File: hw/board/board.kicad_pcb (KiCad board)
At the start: 2 copper layers, 31.8 x 54.6 mm, 4 parts, among them J1 Conn_02x20_Odd_Even, U1 W65C02S

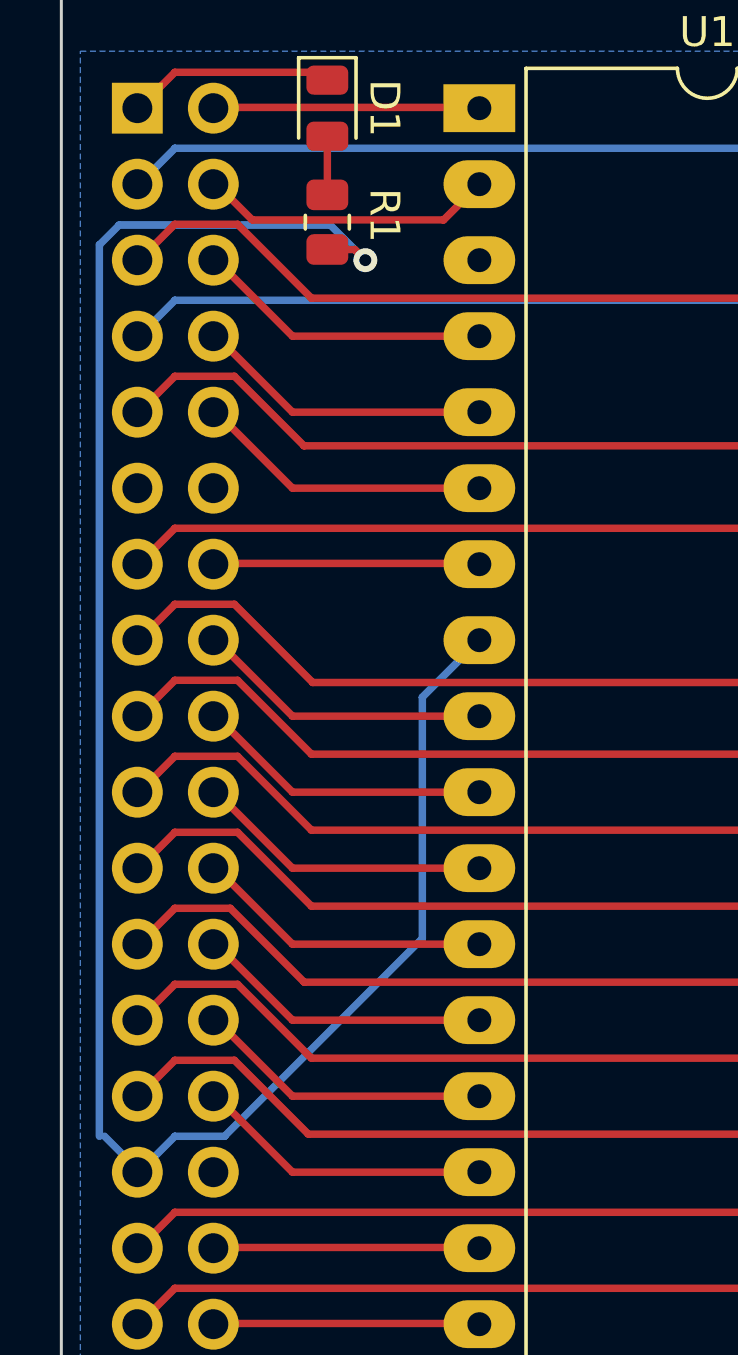
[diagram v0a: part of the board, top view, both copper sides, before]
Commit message: Fix ground plane not connected
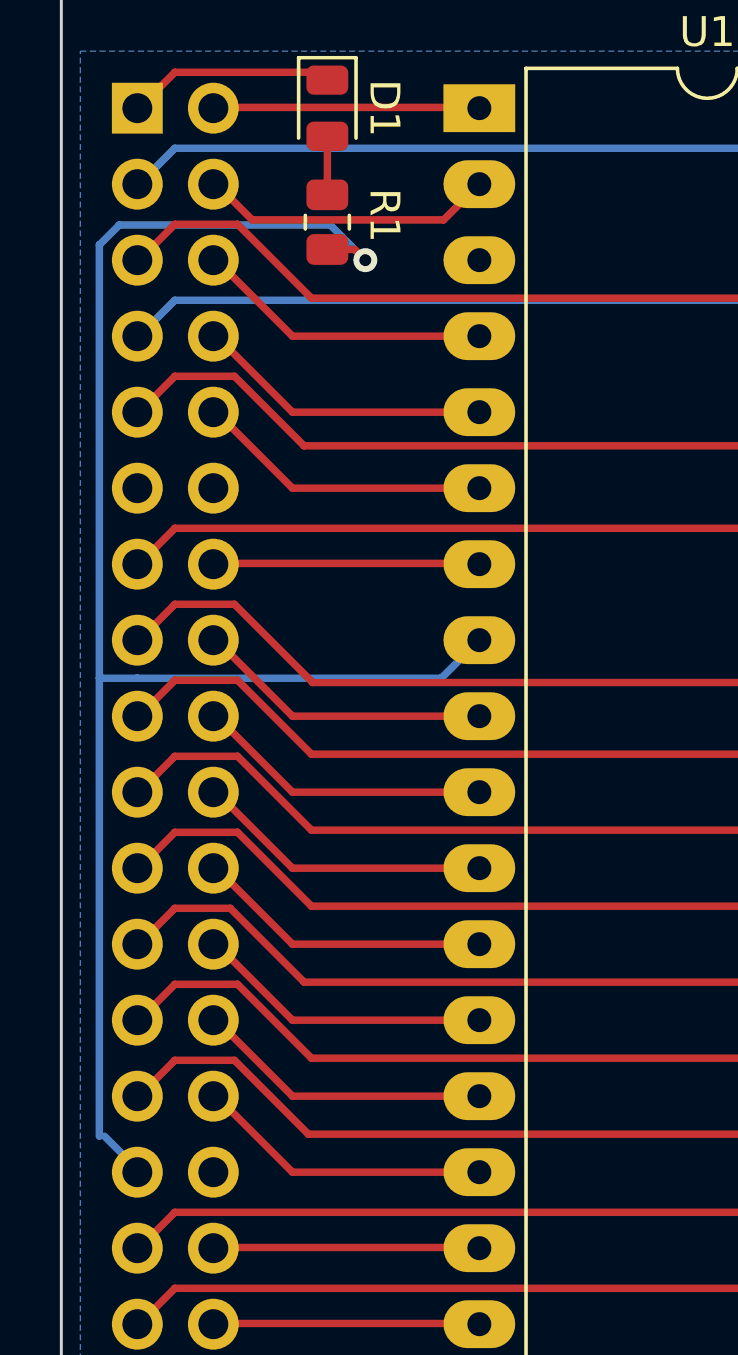
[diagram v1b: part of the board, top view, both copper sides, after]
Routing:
- net +3V3: track 66.0 -> 55.7 mm
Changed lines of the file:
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@@
       (svguseinch false)
       (svgprecision 6)
-      (excludeedgelayer true)
+      (excludeedgelayer false)
       (plotframeref false)
       (viasonmask false)
@@
       (psa4output false)
       (plotreference true)
-      (plotvalue true)
+      (plotvalue false)
       (plotinvisibletext false)
       (sketchpadsonfab false)
-      (subtractmaskfromsilk false)
+      (subtractmaskfromsilk true)
       (outputformat 1)
       (mirror false)
-      (drillshape 1)
+      (drillshape 0)
       (scaleselection 1)
-      (outputdirectory "")
+      (outputdirectory "output/")
     )
   )
@@
     (fp_line (start 1 0.625) (end -1 0.625) (layer "F.Fab") (width 0.1))
     (fp_line (start -1 -0.625) (end 1 -0.625) (layer "F.Fab") (width 0.1))
-    (pad "1" smd roundrect (at -0.9125 0 90) (size 1.025 1.4) (layers "F.Cu" "F.Paste" "F.Mask") (roundrect_rratio 0.243902)
+    (pad "1" smd roundrect (at -0.9125 0 90) (size 1.025 1.4) (layers "F.Cu" "F.Paste" "F.Mask") (roundrect_rratio 0.243902439)
       (net 30 "+3V3") (pintype "passive"))
-    (pad "2" smd roundrect (at 0.9125 0 90) (size 1.025 1.4) (layers "F.Cu" "F.Paste" "F.Mask") (roundrect_rratio 0.243902)
+    (pad "2" smd roundrect (at 0.9125 0 90) (size 1.025 1.4) (layers "F.Cu" "F.Paste" "F.Mask") (roundrect_rratio 0.243902439)
       (net 2 "Net-(D1-Pad2)") (pintype "passive"))
     (model "${KICAD6_3DMODEL_DIR}/Resistor_SMD.3dshapes/R_0805_2012Metric.wrl"
@@
   (segment (start 91.0825 64.4125) (end 91.44 64.77) (width 0.25) (layer "F.Cu") (net 30))
   (via (at 91.44 64.77) (size 0.8) (drill 0.4) (layers "F.Cu" "B.Cu") (net 30))
-  (segment (start 85.074511 94.050489) (end 86.735521 94.050489) (width 0.25) (layer "B.Cu") (net 30))
-  (segment (start 93.345 79.375) (end 95.25 77.47) (width 0.25) (layer "B.Cu") (net 30))
-  (segment (start 86.735521 94.050489) (end 93.345 87.44101) (width 0.25) (layer "B.Cu") (net 30))
+  (segment (start 93.98 78.74) (end 83.82 78.74) (width 0.25) (layer "B.Cu") (net 30))
+  (segment (start 95.25 77.47) (end 93.98 78.74) (width 0.25) (layer "B.Cu") (net 30))
   (segment (start 90.265489 63.595489) (end 91.44 64.77) (width 0.25) (layer "B.Cu") (net 30))
   (segment (start 82.55 64.258501) (end 82.55 94.050489) (width 0.25) (layer "B.Cu") (net 30))
   (segment (start 83.213012 63.595489) (end 90.265489 63.595489) (width 0.25) (layer "B.Cu") (net 30))
+  (segment (start 83.82 78.74) (end 82.55 78.74) (width 0.25) (layer "B.Cu") (net 30))
   (segment (start 82.725489 94.050489) (end 83.9 95.225) (width 0.25) (layer "B.Cu") (net 30))
-  (segment (start 93.345 87.44101) (end 93.345 79.375) (width 0.25) (layer "B.Cu") (net 30))
-  (segment (start 83.9 95.225) (end 85.074511 94.050489) (width 0.25) (layer "B.Cu") (net 30))
   (segment (start 82.55 64.258501) (end 83.213012 63.595489) (width 0.25) (layer "B.Cu") (net 30))
   (segment (start 85.074511 96.590489) (end 109.149511 96.590489) (width 0.25) (layer "F.Cu") (net 31))

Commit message: add basic stuff to board
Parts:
- removed D1: LED, LED_SMD:LED_0805_2012Metric
- added C1: 100n, Capacitor_SMD:C_0603_1608Metric_Pad1.08x0.95mm_HandSolder, B.Cu at (143.3, 59.0)
- added C10: 4.7u, Capacitor_SMD:C_0603_1608Metric_Pad1.08x0.95mm_HandSolder, B.Cu at (106.2, 64.4)
- added C11: 100n, Capacitor_SMD:C_0603_1608Metric_Pad1.08x0.95mm_HandSolder, B.Cu at (107.8, 64.4)
- added C12: 4.7u, Capacitor_SMD:C_0603_1608Metric_Pad1.08x0.95mm_HandSolder, B.Cu at (119.0, 57.4)
- added C13: 100n, Capacitor_SMD:C_0603_1608Metric_Pad1.08x0.95mm_HandSolder, B.Cu at (121.4, 65.2)
- added C14: 100n, Capacitor_SMD:C_0603_1608Metric_Pad1.08x0.95mm_HandSolder, B.Cu at (111.4, 57.4)
- added C15: 100n, Capacitor_SMD:C_0603_1608Metric_Pad1.08x0.95mm_HandSolder, B.Cu at (110.6, 65.5)
- added C16: 4.7u, Capacitor_SMD:C_0603_1608Metric_Pad1.08x0.95mm_HandSolder, F.Cu at (126.8, 59.9)
- added C17: 100n, Capacitor_SMD:C_0603_1608Metric_Pad1.08x0.95mm_HandSolder, B.Cu at (115.0, 68.4)
- added C18: 100n, Capacitor_SMD:C_0603_1608Metric_Pad1.08x0.95mm_HandSolder, B.Cu at (118.4, 68.4)
- added C19: 100n, Capacitor_SMD:C_0603_1608Metric_Pad1.08x0.95mm_HandSolder, B.Cu at (121.4, 61.2)
- added C2: 100n, Capacitor_SMD:C_0603_1608Metric_Pad1.08x0.95mm_HandSolder, B.Cu at (143.4, 63.5)
- added C20: 100n, Capacitor_SMD:C_0603_1608Metric_Pad1.08x0.95mm_HandSolder, B.Cu at (115.6, 57.4)
- added C21: 4.7u, Capacitor_SMD:C_0603_1608Metric_Pad1.08x0.95mm_HandSolder, B.Cu at (106.2, 61.0)
- added C22: 100n, Capacitor_SMD:C_0603_1608Metric_Pad1.08x0.95mm_HandSolder, B.Cu at (107.8, 61.0)
- added C23: 4.7u, Capacitor_SMD:C_0603_1608Metric_Pad1.08x0.95mm_HandSolder, B.Cu at (160.4, 54.4)
- added C24: 0.1u, Capacitor_SMD:C_0603_1608Metric_Pad1.08x0.95mm_HandSolder, B.Cu at (158.8, 54.4)
- added C25: 10u, Capacitor_SMD:C_0603_1608Metric_Pad1.08x0.95mm_HandSolder, F.Cu at (123.8, 26.4)
- added C26: 1u, Capacitor_SMD:C_0603_1608Metric_Pad1.08x0.95mm_HandSolder, F.Cu at (125.3, 26.4)
- added C27: 10n, Capacitor_SMD:C_0603_1608Metric_Pad1.08x0.95mm_HandSolder, F.Cu at (135.8, 24.1)
- added C28: 4.7u, Capacitor_SMD:C_0603_1608Metric_Pad1.08x0.95mm_HandSolder, F.Cu at (119.4, 54.5)
- added C29: 2.2u, Capacitor_SMD:C_0603_1608Metric_Pad1.08x0.95mm_HandSolder, F.Cu at (162.4, 25.6)
- added C3: 100n, Capacitor_SMD:C_0603_1608Metric_Pad1.08x0.95mm_HandSolder, B.Cu at (148.9, 70.0)
- added C30: 1u, Capacitor_SMD:C_0603_1608Metric_Pad1.08x0.95mm_HandSolder, F.Cu at (163.0, 37.9)
- added C31: 100n, Capacitor_SMD:C_0603_1608Metric_Pad1.08x0.95mm_HandSolder, F.Cu at (162.9, 36.2)
- added C32: 10n, Capacitor_SMD:C_0603_1608Metric_Pad1.08x0.95mm_HandSolder, F.Cu at (163.0, 39.5)
- added C33: 0.1u, Capacitor_SMD:C_0603_1608Metric_Pad1.08x0.95mm_HandSolder, F.Cu at (118.6, 51.4)
- added C34: LOAD, Capacitor_SMD:C_0603_1608Metric_Pad1.08x0.95mm_HandSolder, F.Cu at (109.6, 51.8)
- added C35: LOAD, Capacitor_SMD:C_0603_1608Metric_Pad1.08x0.95mm_HandSolder, F.Cu at (104.4, 51.8)
- added C4: 100n, Capacitor_SMD:C_0603_1608Metric_Pad1.08x0.95mm_HandSolder, B.Cu at (152.9, 70.0)
- added C5: 100n, Capacitor_SMD:C_0603_1608Metric_Pad1.08x0.95mm_HandSolder, B.Cu at (159.9, 64.6)
- added C6: 100n, Capacitor_SMD:C_0603_1608Metric_Pad1.08x0.95mm_HandSolder, B.Cu at (159.7, 59.2)
- added C7: 100n, Capacitor_SMD:C_0603_1608Metric_Pad1.08x0.95mm_HandSolder, B.Cu at (152.7, 53.7)
- added C8: 100n, Capacitor_SMD:C_0603_1608Metric_Pad1.08x0.95mm_HandSolder, B.Cu at (151.2, 54.2)
- added C9: 100n, Capacitor_SMD:C_0603_1608Metric_Pad1.08x0.95mm_HandSolder, B.Cu at (149.6, 53.6)
- added L1: 600R @ 100MHz, Inductor_SMD:L_0603_1608Metric_Pad1.05x0.95mm_HandSolder, B.Cu at (104.6, 64.4)
- added L2: 600R @ 100MHz, Inductor_SMD:L_0603_1608Metric_Pad1.05x0.95mm_HandSolder, B.Cu at (104.6, 61.0)
- added L3: 600R @ 100MHz, Inductor_SMD:L_0603_1608Metric_Pad1.05x0.95mm_HandSolder, B.Cu at (157.2, 54.4)
- added R10: 10k, Resistor_SMD:R_0603_1608Metric_Pad0.98x0.95mm_HandSolder, F.Cu at (117.8, 54.5)
- added R11: 4.7k, Resistor_SMD:R_0603_1608Metric_Pad0.98x0.95mm_HandSolder, F.Cu at (116.4, 54.5)
- added R12: 10k, Resistor_SMD:R_0603_1608Metric_Pad0.98x0.95mm_HandSolder, F.Cu at (114.8, 54.5)
- added R2: 5.1k, Resistor_SMD:R_0603_1608Metric_Pad0.98x0.95mm_HandSolder, B.Cu at (94.8, 62.1)
- added R3: 10k, Resistor_SMD:R_0603_1608Metric_Pad0.98x0.95mm_HandSolder, F.Cu at (117.8, 71.5)
- added R4: 12k 1%, Resistor_SMD:R_0603_1608Metric_Pad0.98x0.95mm_HandSolder, B.Cu at (113.6, 61.5)
- added R5: R, Resistor_SMD:R_0603_1608Metric_Pad0.98x0.95mm_HandSolder, F.Cu at (107.5, 65.7)
- added R6: 10k, Resistor_SMD:R_0603_1608Metric_Pad0.98x0.95mm_HandSolder, F.Cu at (120.9, 46.2)
- added R7: 10k, Resistor_SMD:R_0603_1608Metric_Pad0.98x0.95mm_HandSolder, F.Cu at (115.9, 46.5)
- added R8: 10k, Resistor_SMD:R_0603_1608Metric_Pad0.98x0.95mm_HandSolder, F.Cu at (115.9, 50.0)
- added R9: 2.2k, Resistor_SMD:R_0603_1608Metric_Pad0.98x0.95mm_HandSolder, F.Cu at (122.7, 48.9)
- added U2: LD1117S33TR_SOT223, Package_TO_SOT_SMD:SOT-223-3_TabPin2, F.Cu at (130.6, 24.9)
- added U3: LD1117S12TR_SOT223, Package_TO_SOT_SMD:SOT-223-3_TabPin2, F.Cu at (163.8, 30.9)
- added U4: FT2232HL, Package_QFP:LQFP-64_10x10mm_P0.5mm, F.Cu at (116.0, 63.0)
- added U5: 93LCxxBxxOT, Package_TO_SOT_SMD:SOT-23-6, F.Cu at (118.9, 48.8)
- added Y1: 12MHz, Crystal:Crystal_SMD_5032-2Pin_5.0x3.2mm_HandSoldering, F.Cu at (107.0, 54.6)
- J1: value Conn_02x20_Odd_Even -> USB_C_Receptacle_USB2.0; footprint Connector_PinSocket_2.54mm:PinSocket_2x20_P2.54mm_Vertical -> Connector_USB:USB_C_Receptacle_GCT_USB4085; moved to F.Cu
- R1: value 100 -> 5.1k; footprint Resistor_SMD:R_0805_2012Metric -> Resistor_SMD:R_0603_1608Metric_Pad0.98x0.95mm_HandSolder; moved to B.Cu
- U1: value W65C02S -> T8Q144; footprint Package_DIP:DIP-40_W15.24mm_LongPads -> Package_QFP:LQFP-144_20x20mm_P0.5mm
- moved U1 56.4 mm to (151.7, 61.8)
- moved J1 13.7 mm to (97.5, 58.8), turned to -90 degrees
- moved R1 10.3 mm to (100.0, 60.5), turned to 0 degrees
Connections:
- R1 pad 1: +3V3 -> Net-(J1-PadA5)
- R1 pad 2: Net-(D1-Pad2) -> GND
- U1 pad 1: /VPB -> GND
- U1 pad 10: /A1 -> unconnected-(U1-Pad10)
- U1 pad 11: /A2 -> unconnected-(U1-Pad11)
- U1 pad 12: /A3 -> +3V3
- U1 pad 13: /A4 -> +1V2
- U1 pad 14: /A5 -> unconnected-(U1-Pad14)
- U1 pad 15: /A6 -> unconnected-(U1-Pad15)
- U1 pad 16: /A7 -> unconnected-(U1-Pad16)
- U1 pad 17: /A8 -> unconnected-(U1-Pad17)
- U1 pad 18: /A9 -> unconnected-(U1-Pad18)
- U1 pad 19: /A10 -> unconnected-(U1-Pad19)
- U1 pad 2: /RDY -> Net-(C23-Pad1)
- U1 pad 20: /A11 -> unconnected-(U1-Pad20)
- U1 pad 21: GND -> +3V3
- U1 pad 22: /A12 -> +1V2
- U1 pad 23: /A13 -> +3V3
- U1 pad 24: /A14 -> unconnected-(U1-Pad24)
- U1 pad 25: /A15 -> unconnected-(U1-Pad25)
- U1 pad 26: /D7 -> unconnected-(U1-Pad26)
- U1 pad 27: /D6 -> unconnected-(U1-Pad27)
- U1 pad 28: /D5 -> unconnected-(U1-Pad28)
- U1 pad 29: /D4 -> unconnected-(U1-Pad29)
- U1 pad 30: /D3 -> unconnected-(U1-Pad30)
- U1 pad 31: /D2 -> unconnected-(U1-Pad31)
- U1 pad 32: /D1 -> unconnected-(U1-Pad32)
- U1 pad 33: /D0 -> unconnected-(U1-Pad33)
- U1 pad 34: /R~{WB} -> unconnected-(U1-Pad34)
- U1 pad 36: /BE -> unconnected-(U1-Pad36)
- U1 pad 37: /PHI2 -> GND
- U1 pad 38: /~{SOB} -> unconnected-(U1-Pad38)
- U1 pad 4: /~{IRQB} -> unconnected-(U1-Pad4)
- U1 pad 40: /~{RESB} -> unconnected-(U1-Pad40)
- U1 pad 5: /~{MLB} -> GND
- U1 pad 6: /~{NMIB} -> unconnected-(U1-Pad6)
- U1 pad 7: /SYNC -> unconnected-(U1-Pad7)
- U1 pad 8: +3V3 -> unconnected-(U1-Pad8)
- U1 pad 9: /A0 -> GND
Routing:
- net GND: track 0.00 -> 69.8 mm, vias 0 -> 37
- net Net-(C23-Pad1): track 0.00 -> 49.3 mm, vias 0 -> 3
- net +1V2: track 0.00 -> 37.4 mm, vias 0 -> 16
- net +3V3: track 55.7 -> 24.0 mm, vias 1 -> 8
- net Net-(R6-Pad2): track 0.00 -> 29.7 mm
- net /D0: track 28.7 -> 0.00 mm
- net /D4: track 28.6 -> 0.00 mm
- net /~{SOB}: track 28.6 -> 0.00 mm
- net /D2: track 28.6 -> 0.00 mm
- net /D6: track 28.6 -> 0.00 mm
- net /D3: track 28.6 -> 0.00 mm
- net /D1: track 28.6 -> 0.00 mm
- net /D5: track 28.6 -> 0.00 mm
- net /BE: track 28.5 -> 0.00 mm
- net /~{RESB}: track 27.6 -> 0.00 mm
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- added copper zone on F.Cu, net +1V2
- added copper zone on In1.Cu, net +1V2
- added copper zone on In1.Cu, net /VRO
- added copper zone on F.Cu, net GND
- added copper zone on In2.Cu, net GND
- removed copper zone on B.Cu, net GND
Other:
- board outline removed
- copper layers 2 -> 4
